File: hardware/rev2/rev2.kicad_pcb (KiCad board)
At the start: 4 copper layers, 60 x 40 mm, 142 parts, among them J1 USB_C_Receptacle_USB2.0_16P, J2 uFL, J3 uFL, J4 Antenna RF and GNSS Data, J5 Antenna GND, J6 uFL, J8 Battery Connection, Q1 SS8050, SW1 SW_Push, SW2 SW_Push, U1 EClamp2522P, U2 ESP32-S3FN8, U3 SX1262IMLTRT, U4 PE4259, U5 MP2664GG-xxxx-P, U6 MAX17055ETB+, U8 TPS631000DRLR, Y1 ECS-2520SMV-400-FN-TR, Y2 TXO-20CSMV-320

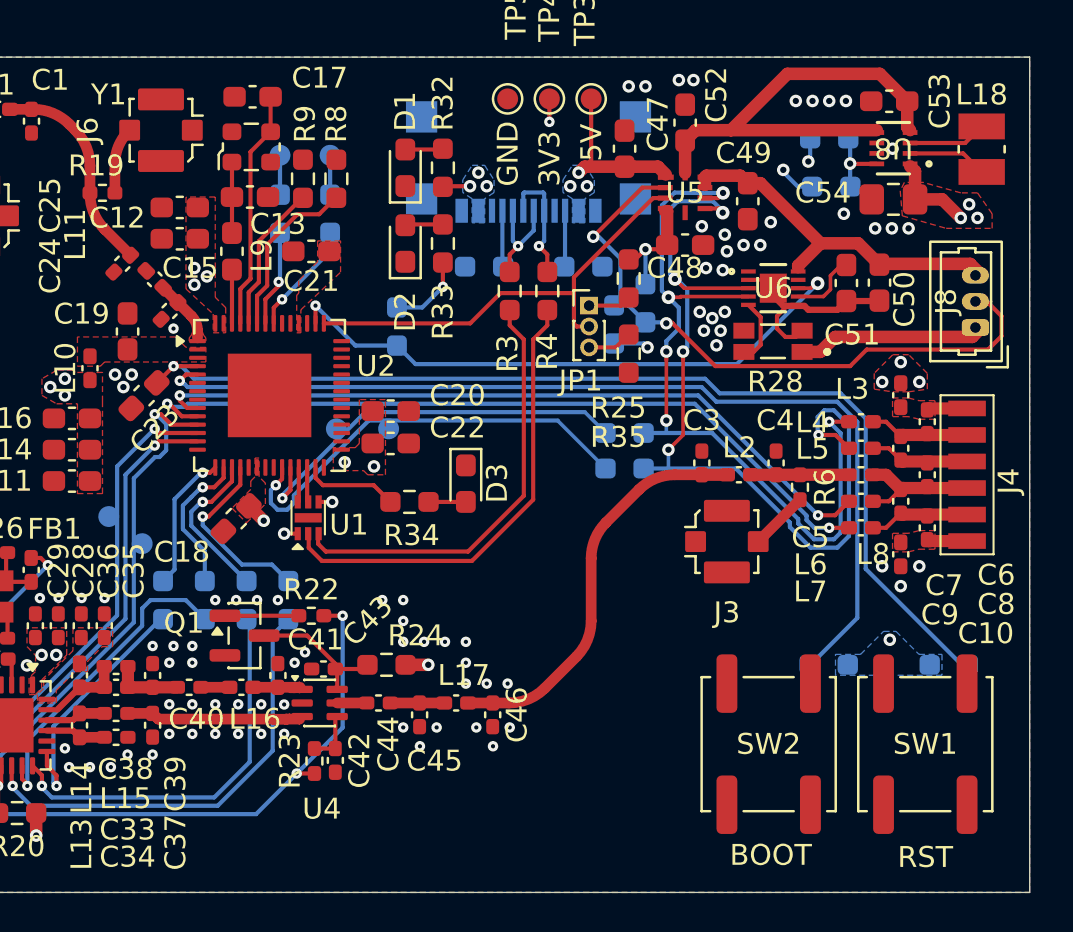
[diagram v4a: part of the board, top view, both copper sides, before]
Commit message: fixed some drc issues and layout review
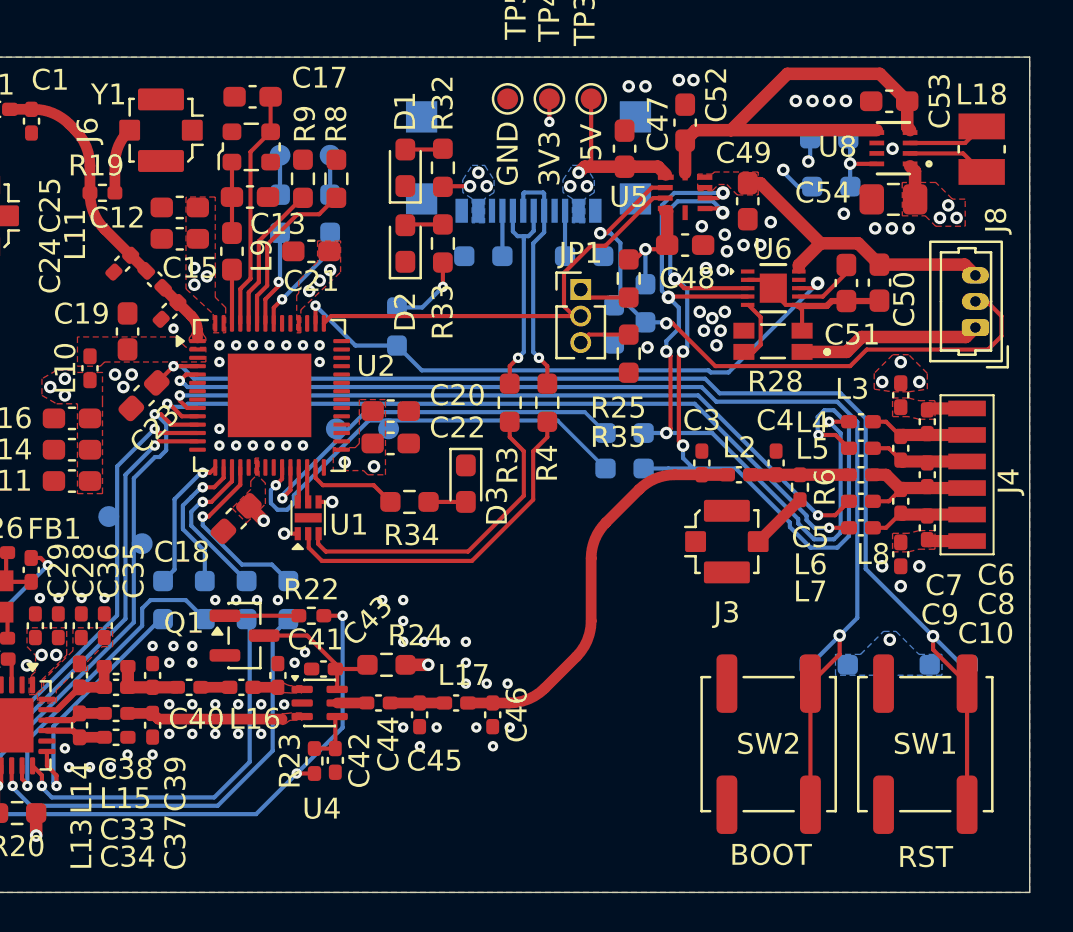
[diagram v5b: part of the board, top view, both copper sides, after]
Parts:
- JP1: footprint Connector_PinHeader_1.00mm:PinHeader_1x03_P1.00mm_Vertical -> Connector_PinHeader_1.27mm:PinHeader_1x03_P1.27mm_Vertical
- moved R3 5.35 mm to (163.1, 73.5)
- moved R4 5.35 mm to (164.9, 73.5)
- moved JP1 0.87 mm to (166.5, 68.1)
- moved R1 0.50 mm to (161.8, 66.5)
- moved R2 0.50 mm to (166.7, 66.5)
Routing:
- net Net-(U2-CHIP_PU): track 50.3 -> 59.1 mm, vias 1 -> 2
- net /ESP32/GPIO0: track 46.8 -> 55.5 mm, vias 1 -> 2
- net /D+: track 5.89 -> 11.5 mm
- net /*D+: track 22.3 -> 16.9 mm
- net /*D-: track 20.8 -> 15.4 mm
- net /D-: track 5.20 -> 10.5 mm
- net /Power/BATT+: track 17.2 -> 14.4 mm
- net +3V3: track 14.7 -> 12.1 mm, vias 26 -> 29
- net /Power/CSP: track 10.0 -> 8.34 mm
- net GND: track 2.53 -> 1.14 mm, vias 94 -> 109
- net Net-(U4-RF1): track 2.24 -> 1.18 mm
- net /Antenna_WiFi: track 10.3 -> 11.3 mm
- net Net-(U4-RF2): track 8.34 -> 7.50 mm
- net Net-(J1-CC2): track 2.67 -> 2.17 mm
- net Net-(J1-CC1): track 2.67 -> 2.17 mm
- added copper zone on F.Cu, net /Power/BATT+

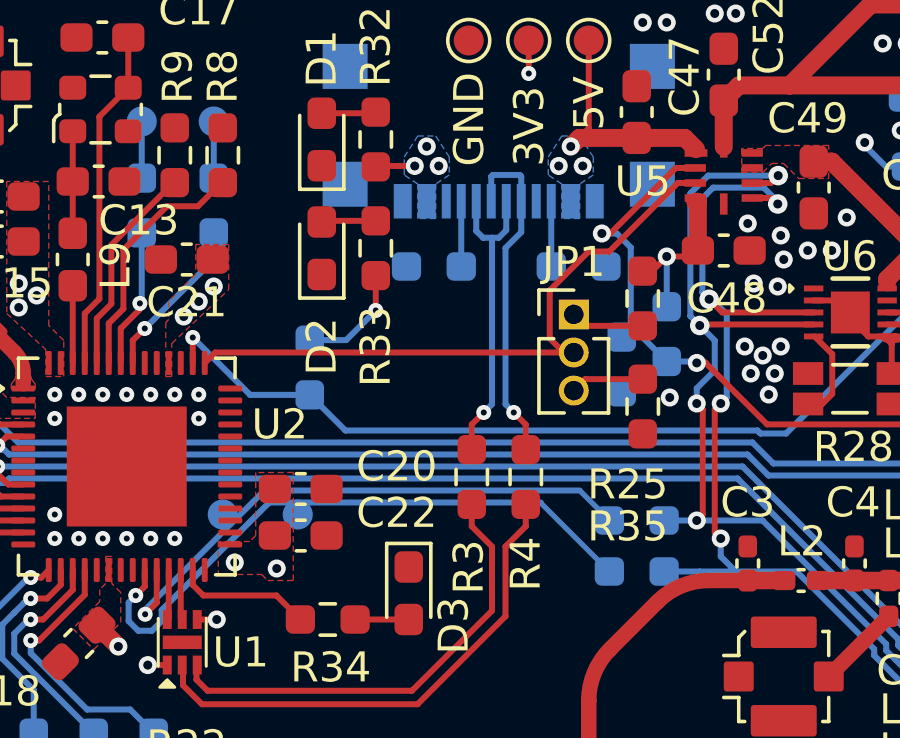
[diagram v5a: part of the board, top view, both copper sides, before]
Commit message: Replaced charger wake-up cap jumper headers
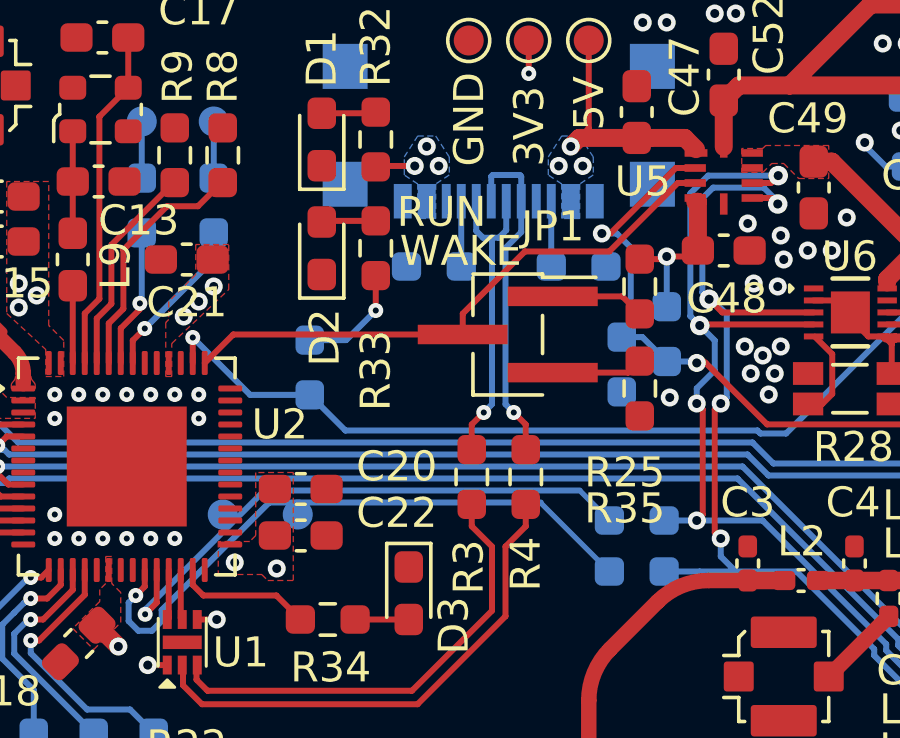
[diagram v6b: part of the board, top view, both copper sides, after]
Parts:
- JP1: footprint Connector_PinHeader_1.27mm:PinHeader_1x03_P1.27mm_Vertical -> Connector_PinHeader_1.27mm:PinHeader_1x03_P1.27mm_Vertical_SMD_Pin1Right
- R26: value TBD -> 11.5kΩ
- R27: value TBD -> 309kΩ
- R31, R35: value TBD -> 10kΩ
- moved JP1 2.30 mm to (164.3, 68.8)
- moved R35 0.61 mm to (168.7, 70.6)
- moved R25 0.41 mm to (168.7, 67.2)
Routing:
- net /Power/INT: track 21.4 -> 19.2 mm
- net Net-(JP1-A): track 2.46 -> 3.14 mm
- net Net-(JP1-B): track 2.46 -> 3.06 mm
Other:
- board text added: "RUN"
- board text added: "WAKE"

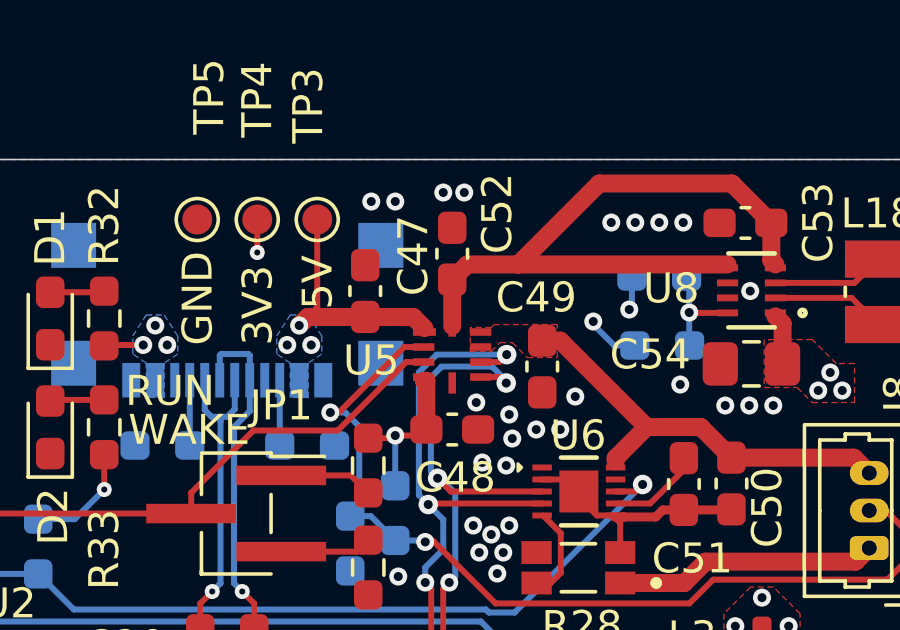
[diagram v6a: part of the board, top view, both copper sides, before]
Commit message: Added a few GND vias
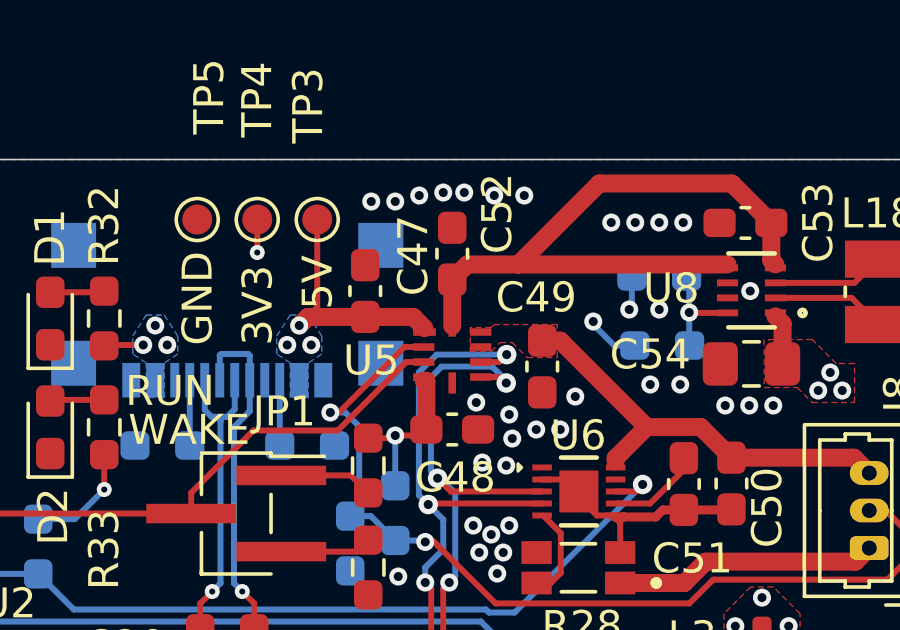
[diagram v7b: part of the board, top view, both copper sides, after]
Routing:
- net GND: vias 109 -> 114
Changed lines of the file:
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@@
 		(tags "Surface mounted pin header SMD 1x03 1.27mm single row style2 pin1 right")
 		(property "Reference" "JP1"
-			(at 1.5 -3.6 0)
+			(at 1.6 -3.4 0)
 			(layer "F.SilkS")
 			(effects
@@
 	)
 	(via
+		(at 170.4 58.2)
+		(size 0.6)
+		(drill 0.3)
+		(layers "F.Cu" "B.Cu")
+		(net "GND")
+	)
+	(via
 		(at 133 91)
 		(size 0.5)
@@
 	)
 	(via
+		(at 178.4 62)
+		(size 0.6)
+		(drill 0.3)
+		(layers "F.Cu" "B.Cu")
+		(net "GND")
+	)
+	(via
 		(at 163 87)
 		(size 0.5)
@@
 	)
 	(via
+		(at 172.9 58.2)
+		(size 0.6)
+		(drill 0.3)
+		(layers "F.Cu" "B.Cu")
+		(net "GND")
+	)
+	(via
 		(at 158.8 90)
 		(size 0.5)
@@
 	)
 	(via
+		(at 178.1 64.5)
+		(size 0.6)
+		(drill 0.3)
+		(layers "F.Cu" "B.Cu")
+		(net "GND")
+	)
+	(via
 		(at 173.4 65.5)
 		(size 0.6)
@@
 		(net "GND")
 	)
+	(via
+		(at 173.9 58.2)
+		(size 0.6)
+		(drill 0.3)
+		(layers "F.Cu" "B.Cu")
+		(net "GND")
+	)

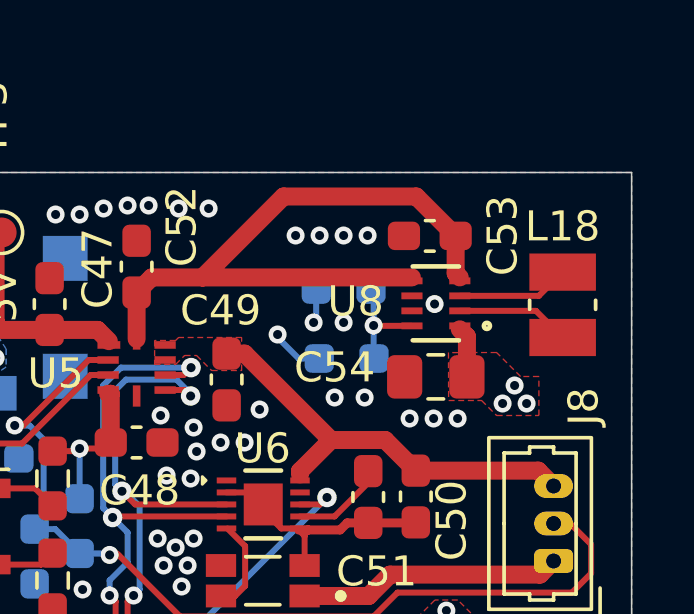
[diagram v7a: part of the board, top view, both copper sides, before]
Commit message: Moved the buck-boost inductor a bit closer to the buck-boost IC
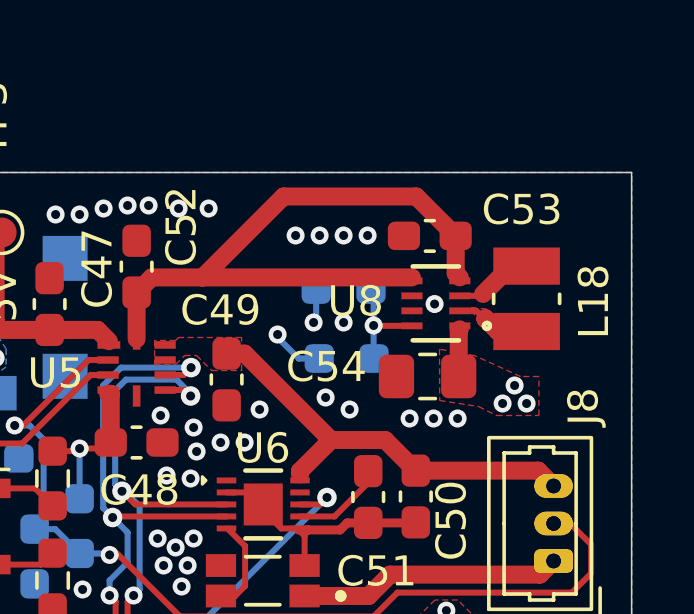
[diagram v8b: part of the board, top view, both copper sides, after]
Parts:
- moved L18 1.22 mm to (184.5, 61.2)
- moved C54 0.27 mm to (181.2, 63.8)
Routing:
- net Net-(U8-LX2): track 3.79 -> 2.53 mm
- net Net-(U8-LX1): track 3.76 -> 2.64 mm
- added copper zone on F.Cu, net Net-(U8-LX2)
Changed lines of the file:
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@@
 	(footprint "_footprints:INDC2520X120N"
 		(layer "F.Cu")
-		(at 185.7 61.41 -90)
+		(at 184.5 61.21 -90)
 		(property "Reference" "L18"
-			(at -2.61 0 180)
+			(at 0.09 -2.25 270)
 			(layer "F.SilkS")
 			(effects
@@
 	(footprint "Capacitor_SMD:C_0805_2012Metric_Pad1.18x1.45mm_HandSolder"
 		(layer "F.Cu")
-		(at 181.472701 63.8123 180)
+		(at 181.2 63.8 180)
 		(descr "Capacitor SMD 0805 (2012 Metric), square (rectangular) end terminal, IPC-7351 nominal with elongated pad for handsoldering. (Body size source: IPC-SM-782 page 76, https://www.pcb-3d.com/wordpress/wp-content/uploads/ipc-sm-782a_amendment_1_and_2.pdf, https://docs.google.com/spreadsheets/d/1BsfQQcO9C6DZCsRaXUlFlo91Tg2WpOkGARC1WS5S8t0/edit?usp=sharing)")
 		(tags "capacitor handsolder")
@@
 		(tags "capacitor handsolder")
 		(property "Reference" "C53"
-			(at -2.427299 0.0123 90)
+			(at -3.077299 0.8623 180)
 			(layer "F.SilkS")
 			(effects
@@
 	)
 	(via
-		(at 178.1 64.5)
+		(at 177.8 64.5)
 		(size 0.6)
 		(drill 0.3)
@@
 	)
 	(via
-		(at 179.1 64.5)
+		(at 178.6 64.9)
 		(size 0.6)
 		(drill 0.3)
@@
 	)
 	(segment
-		(start 182.510201 63.8123)
-		(end 182.510201 62.4645)
+		(start 182.2375 63.8)
+		(end 182.2375 62.262201)
+		(width 0.6)
+		(layer "F.Cu")
+		(net "+3V3")
+	)
+	(segment
+		(start 182.2375 62.262201)
+		(end 182.272701 62.227)
 		(width 0.6)
 		(layer "F.Cu")
@@
 	)
 	(segment
-		(start 182.510201 62.4645)
-		(end 182.272701 62.227)
-		(width 0.6)
-		(layer "F.Cu")
-		(net "+3V3")
-	)
-	(segment
 		(start 153.95 78.299999)
 		(end 154.6 78.299998)
@@
 	)
 	(segment
-		(start 185.7 62.5)
-		(end 184.8123 61.6123)
+		(start 182.272701 61.6123)
+		(end 182.8259 61.6123)
+		(width 0.2)
+		(layer "F.Cu")
+		(net "Net-(U8-LX2)")
+	)
+	(segment
+		(start 182.8259 61.6123)
+		(end 183.0636 61.85)
 		(width 0.2)
 		(layer "F.Cu")
@@
 	)
 	(segment
-		(start 184.8123 61.6123)
-		(end 182.272701 61.6123)
+		(start 184.5 62.3)
+		(end 183.55 62.3)
+		(width 0.6)
+		(layer "F.Cu")
+		(net "Net-(U8-LX2)")
+	)
+	(segment
+		(start 183.0636 61.85)
+		(end 183.1259 61.85)
 		(width 0.2)
 		(layer "F.Cu")
@@
 	)
 	(segment
-		(start 185.7 60.32)
-		(end 184.9077 61.1123)
+		(start 183.55 62.3)
+		(end 183.1259 61.8759)
+		(width 0.6)
+		(layer "F.Cu")
+		(net "Net-(U8-LX2)")
+	)
+	(segment
+		(start 183.1259 61.8759)
+		(end 183.1259 61.85)
+		(width 0.6)
+		(layer "F.Cu")
+		(net "Net-(U8-LX2)")
+	)
+	(segment
+		(start 182.9877 61.1123)
+		(end 183.05 61.05)
 		(width 0.2)
 		(layer "F.Cu")
@@
 	)
 	(segment
-		(start 184.9077 61.1123)
-		(end 182.272701 61.1123)
+		(start 183.98 60.12)
+		(end 183.05 61.05)
+		(width 0.6)
+		(layer "F.Cu")
+		(net "Net-(U8-LX1)")
+	)
+	(segment
+		(start 182.272701 61.1123)
+		(end 182.9877 61.1123)
 		(width 0.2)
 		(layer "F.Cu")
@@
 	)
 	(segment
+		(start 184.5 60.12)
+		(end 183.98 60.12)
+		(width 0.6)
+		(layer "F.Cu")
+		(net "Net-(U8-LX1)")
+	)
+	(segment
 		(start 179.412301 62.112301)
 		(end 179.4 62.1)
@@
 		(polygon
 			(pts
-				(xy 183 64.6) (xy 183.500147 65.100147) (xy 184.910956 65.099112) (xy 184.91 63.799996) (xy 184.3 63.8)
-				(xy 183.501212 63.001212) (xy 181.895111 63.003997) (xy 181.9 64.6)
+				(xy 182.9 64.8) (xy 183.500147 65.100147) (xy 184.910956 65.099112) (xy 184.91 63.799996) (xy 184.3 63.8)
+				(xy 182.772081 63.105492) (xy 181.59721 62.888846) (xy 181.602452 64.6)
 			)
 		)
@@
 			)
 		)
+	)
+	(zone
+		(net "Net-(U8-LX2)")
+		(layer "F.Cu")
+		(hatch edge 0.5)
+		(priority 24)
+		(connect_pads yes
+			(clearance 0.15)
+		)
+		(min_thickness 0.25)
+		(fill yes
+			(thermal_gap 0.5)
+			(thermal_bridge_width 0.5)
+			(island_removal_mode 0)
+		)
+		(polygon
+			(pts
+				(xy 182.65 61.5) (xy 183.15 61.55) (xy 183.35 61.7) (xy 182.9 62.05) (xy 182.75 61.7) (xy 182.65 61.7)
+			)
+		)
